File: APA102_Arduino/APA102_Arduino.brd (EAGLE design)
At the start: 39.4 x 32.8 mm, 16 parts, among them J1 POWER_JACKSMD, U1 V_REG_LD1117, U2 ATMEGA328P-PU

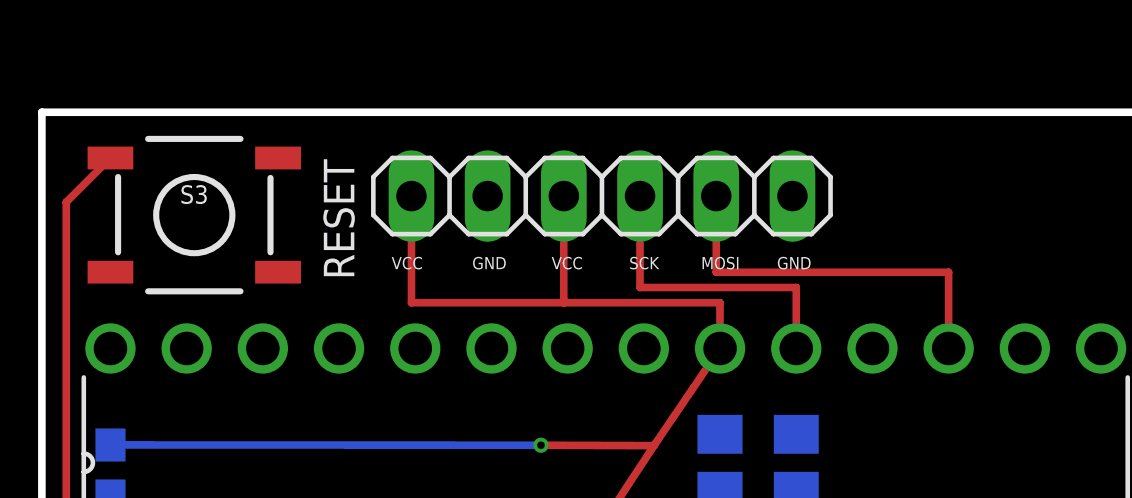
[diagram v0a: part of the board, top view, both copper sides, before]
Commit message: Updated design to use the 6-pin header autogenerated from Library.IO that includes a 3D package.
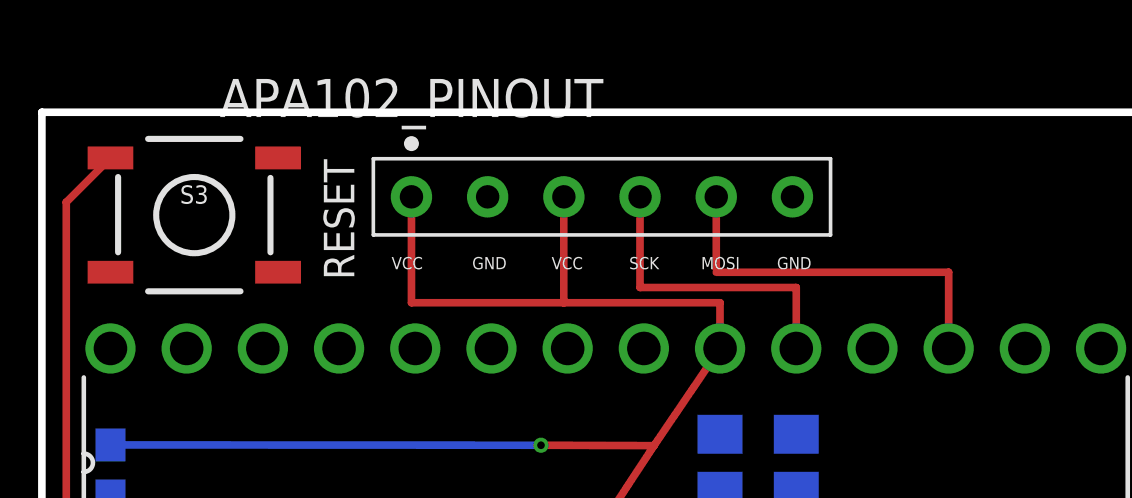
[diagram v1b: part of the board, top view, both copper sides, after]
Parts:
- APA102_PINOUT: value (none) -> 929974-01-06-RK9; device pinhead:1X06 -> SamacSys_Parts:929974-01-06-RK
- moved APA102_PINOUT 6.35 mm to (12.3, 29.9)

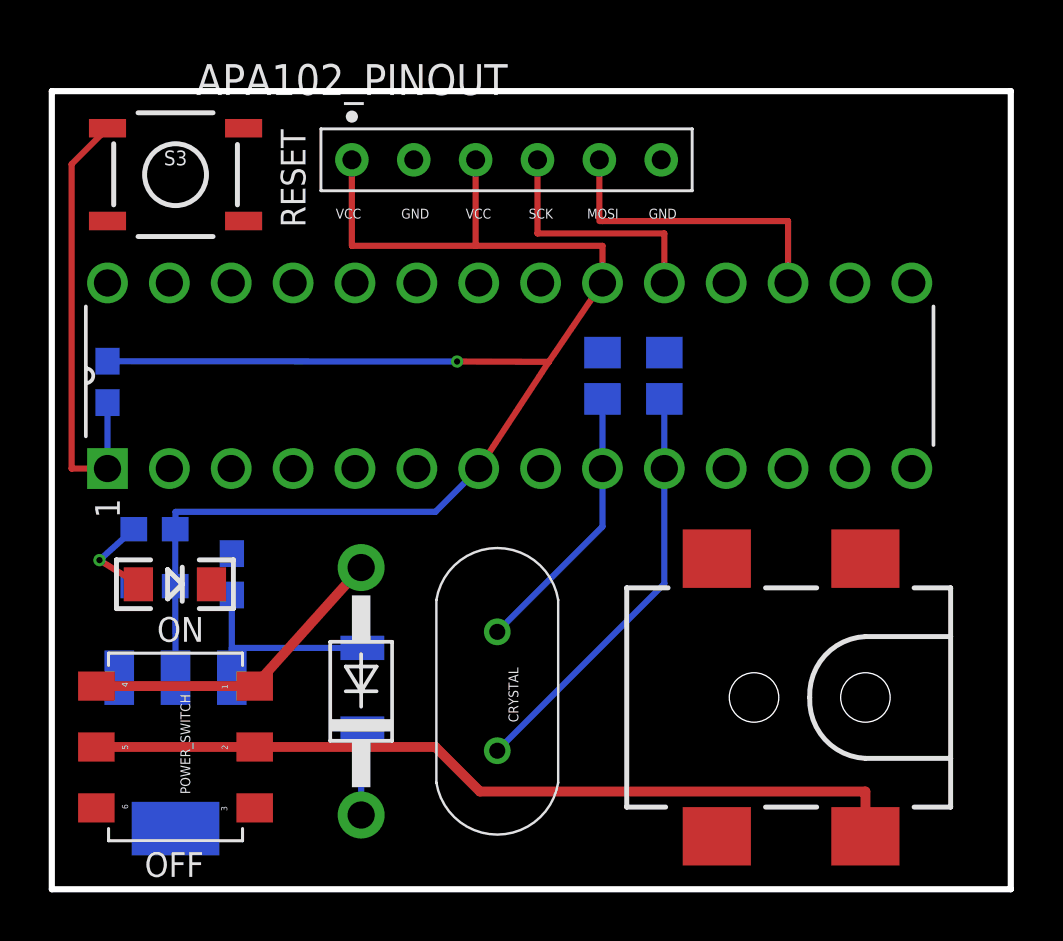
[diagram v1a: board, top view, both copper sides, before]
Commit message: Updated to include devices containing 3D Objects for crystal and power jack.
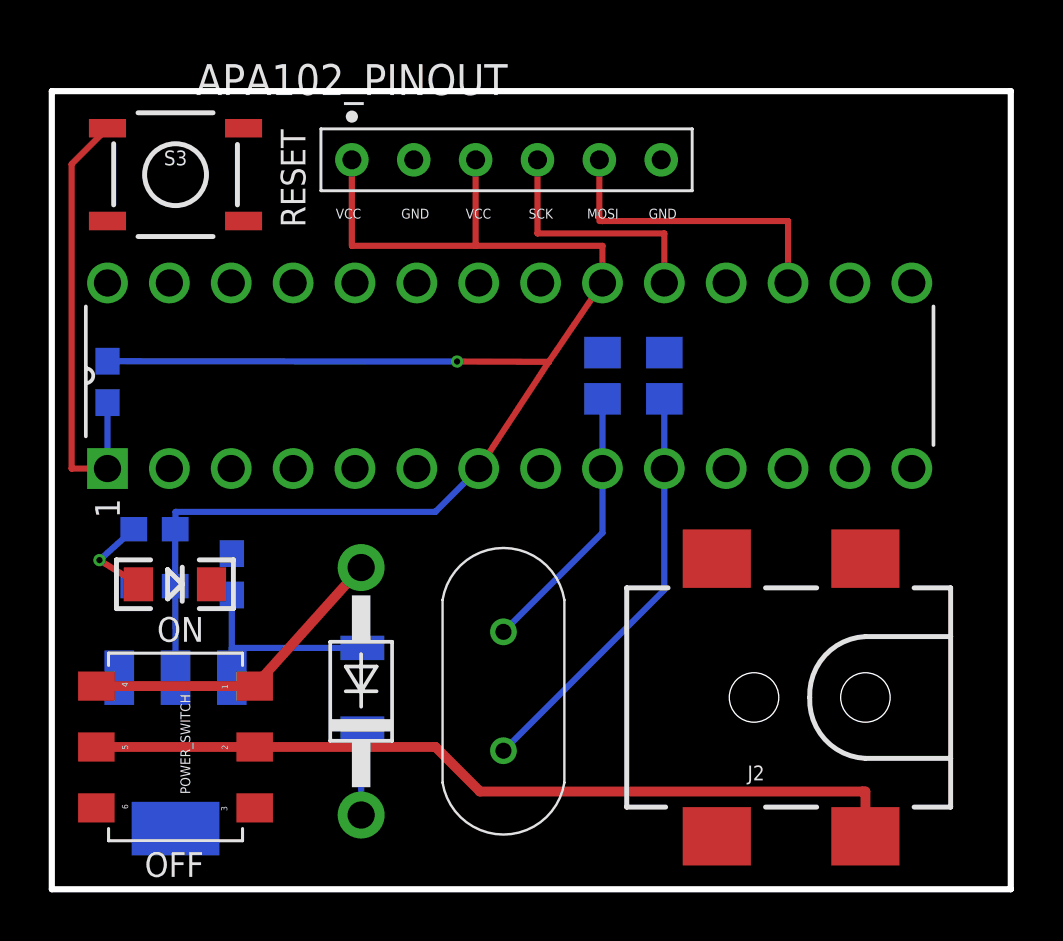
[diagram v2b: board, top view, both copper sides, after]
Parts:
- removed CRYSTAL: 16MHZ, SamacSys_Parts:HC/49US_(AT49)PTH
- removed J1: POWER_JACKSMD, SparkFun-Connectors:POWER_JACK_SMD
- added J2: POWER_JACKPOWER_JACK_SMD, Magister-Libraries:POWER_JACK_SMD
- added Y1: ABL-16.000MHZ-B4Y, Magister-Libraries:HC/49US_(AT49)PTH
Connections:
- net GND: now also J2.GND, J2.P$4; no longer J1.GND, J1.P$4
- net N$3: now also Y1.1; no longer CRYSTAL.2
- net N$6: now also Y1.2; no longer CRYSTAL.1
- net VIN: now also J2.VIN0; no longer J1.VIN0
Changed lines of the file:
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@@
 <drawing>
 <settings>
-<setting alwaysvectorfont="no"/>
+<setting alwaysvectorfont="yes"/>
 <setting keepoldvectorfont="yes"/>
 <setting verticaltext="up"/>
@@
 <layer number="59" name="tCarbon" color="7" fill="1" visible="no" active="no"/>
 <layer number="60" name="bCarbon" color="7" fill="1" visible="no" active="no"/>
+<layer number="88" name="SimResults" color="9" fill="1" visible="no" active="no"/>
+<layer number="89" name="SimProbes" color="9" fill="1" visible="no" active="no"/>
 <layer number="90" name="Modules" color="5" fill="1" visible="no" active="no"/>
 <layer number="91" name="Nets" color="2" fill="1" visible="no" active="no"/>
@@
 <layer number="112" name="tSilk" color="7" fill="1" visible="no" active="no"/>
 <layer number="113" name="IDFDebug" color="4" fill="1" visible="no" active="no"/>
+<layer number="114" name="Badge_Outline" color="7" fill="1" visible="no" active="no"/>
+<layer number="115" name="ReferenceISLANDS" color="7" fill="1" visible="no" active="no"/>
 <layer number="116" name="Patch_BOT" color="9" fill="4" visible="yes" active="yes"/>
+<layer number="117" name="PM_Ref" color="7" fill="1" visible="no" active="no"/>
 <layer number="118" name="Rect_Pads" color="7" fill="1" visible="no" active="no"/>
+<layer number="119" name="PF_Ref" color="7" fill="1" visible="no" active="no"/>
+<layer number="120" name="WFL_Ref" color="7" fill="1" visible="no" active="no"/>
 <layer number="121" name="_tsilk" color="7" fill="1" visible="yes" active="yes"/>
 <layer number="122" name="_bsilk" color="7" fill="1" visible="yes" active="yes"/>
@@
 <attribute name="VALUE" x="11.176" y="6.985" size="0.4064" layer="28" rot="MR90"/>
 </element>
-<element name="J1" library="SparkFun-Connectors" package="POWER_JACK_SMD" value="POWER_JACKSMD" x="33.401" y="7.874" smashed="yes" rot="R180">
-<attribute name="PROD_ID" value="CONN-08106" x="33.401" y="7.874" size="1.778" layer="27" rot="R180" display="off"/>
-</element>
 <element name="U2" library="ATMEGA328P-PU" package="DIP254P762X457-28" value="ATMEGA328P-PU" x="35.306" y="24.892" smashed="yes" rot="R90">
 <attribute name="AVAILABILITY" value="Unavailable" x="35.306" y="24.892" size="1.778" layer="27" rot="R90" display="off"/>
@@
 <attribute name="VALUE" x="27.5082" y="21.844" size="0.4064" layer="28" rot="MR270"/>
 </element>
-<element name="CRYSTAL" library="SamacSys_Parts" package="HC/49US_(AT49)PTH" value="16MHZ" x="18.288" y="8.128" smashed="yes" rot="R90">
-<attribute name="DESCRIPTION" value="Crystals 16.000MHZ, 18pF 30ppm -20C +70C" x="18.288" y="8.128" size="1.778" layer="27" rot="R90" display="off"/>
-<attribute name="HEIGHT" value="mm" x="18.288" y="8.128" size="1.778" layer="27" rot="R90" display="off"/>
-<attribute name="MANUFACTURER_NAME" value="ABRACON" x="18.288" y="8.128" size="1.778" layer="27" rot="R90" display="off"/>
-<attribute name="MANUFACTURER_PART_NUMBER" value="ABL-16.000MHz-B4Y" x="18.288" y="8.128" size="1.778" layer="27" rot="R90" display="off"/>
-<attribute name="MOUSER_PART_NUMBER" value="815-ABL-16-B4Y" x="18.288" y="8.128" size="1.778" layer="27" rot="R90" display="off"/>
-<attribute name="MOUSER_PRICE-STOCK" value="https://www.mouser.co.uk/ProductDetail/ABRACON/ABL-16000MHz-B4Y?qs=DZ%2FvJMgWWIsyUPmWNxNaQw%3D%3D" x="18.288" y="8.128" size="1.778" layer="27" rot="R90" display="off"/>
-<attribute name="NAME" x="18.9508" y="7.9822" size="0.4064" layer="25" rot="R270" align="center"/>
-<attribute name="RS_PART_NUMBER" value="" x="18.288" y="8.128" size="1.778" layer="27" rot="R90" display="off"/>
-<attribute name="RS_PRICE-STOCK" value="" x="18.288" y="8.128" size="1.778" layer="27" rot="R90" display="off"/>
-<attribute name="VALUE" x="18.3158" y="8.0584" size="0.4064" layer="27" rot="R270" align="center"/>
-</element>
 <element name="R5" library="SparkFun" package="0603-RES" value="10K" x="2.286" y="20.828" smashed="yes" rot="MR270">
 <attribute name="NAME" x="2.5146" y="22.4536" size="0.4064" layer="26" font="vector" rot="MR0"/>
@@
 <attribute name="VALUE" x="7.747" y="26.7716" size="1.27" layer="27" align="top-center"/>
 </element>
+<element name="Y1" library="Magister-Libraries" library_urn="urn:adsk.eagle:library:23190065" package="HC/49US_(AT49)PTH" package3d_urn="urn:adsk.eagle:package:23090764/3" value="ABL-16.000MHZ-B4Y" x="18.542" y="8.128" smashed="yes" rot="R270">
+<attribute name="DESCRIPTION" value="Crystals 16.000MHZ, 18pF 30ppm -20C +70C" x="18.542" y="8.128" size="1.778" layer="27" rot="R270" display="off"/>
+<attribute name="HEIGHT" value="mm" x="18.542" y="8.128" size="1.778" layer="27" rot="R270" display="off"/>
+<attribute name="MANUFACTURER_NAME" value="ABRACON" x="18.542" y="8.128" size="1.778" layer="27" rot="R270" display="off"/>
+<attribute name="MANUFACTURER_PART_NUMBER" value="ABL-16.000MHz-B4Y" x="18.542" y="8.128" size="1.778" layer="27" rot="R270" display="off"/>
+<attribute name="MOUSER_PART_NUMBER" value="815-ABL-16-B4Y" x="18.542" y="8.128" size="1.778" layer="27" rot="R270" display="off"/>
+<attribute name="MOUSER_PRICE-STOCK" value="https://www.mouser.co.uk/ProductDetail/ABRACON/ABL-16000MHz-B4Y?qs=DZ%2FvJMgWWIsyUPmWNxNaQw%3D%3D" x="18.542" y="8.128" size="1.778" layer="27" rot="R270" display="off"/>
+</element>
+<element name="J2" library="Magister-Libraries" library_urn="urn:adsk.eagle:library:23190065" package="POWER_JACK_SMD" package3d_urn="urn:adsk.eagle:package:23235900/2" value="POWER_JACKPOWER_JACK_SMD" x="33.401" y="7.874" smashed="yes" rot="R180">
+<attribute name="NAME" x="29.2608" y="5.08" size="0.6096" layer="25" font="vector" ratio="20" rot="R180"/>
+<attribute name="VALUE" x="29.591" y="11.176" size="0.6096" layer="27" font="vector" ratio="20" rot="R180"/>
+</element>
 </elements>
 <signals>
 <signal name="GND">
 <contactref element="LED2" pad="C"/>
-<contactref element="J1" pad="P$4"/>
-<contactref element="J1" pad="GND"/>
 <polygon width="0.254" layer="16" isolate="0.3048">
 <vertex x="0" y="32.766"/>
@@
 <contactref element="APA102_PINOUT" pad="2"/>
 <contactref element="APA102_PINOUT" pad="6"/>
+<contactref element="J2" pad="P$4"/>
+<contactref element="J2" pad="GND"/>
 </signal>
 <signal name="N$8">
@@
 </signal>
 <signal name="VIN">
-<contactref element="J1" pad="VIN0"/>
 <contactref element="POWER_SWITCH" pad="P2"/>
 <contactref element="POWER_SWITCH" pad="P5"/>
@@
 <wire x1="8.33" y1="5.842" x2="15.748" y2="5.842" width="0.4064" layer="1"/>
 <wire x1="15.748" y1="5.842" x2="17.5768" y2="4.0132" width="0.4064" layer="1"/>
-<wire x1="17.5768" y1="4.0132" x2="33.401" y2="4.0132" width="0.4064" layer="1"/>
+<wire x1="17.5768" y1="4.0132" x2="33.274" y2="4.0132" width="0.4064" layer="1"/>
+<contactref element="J2" pad="VIN0"/>
+<wire x1="33.274" y1="4.0132" x2="33.401" y2="4.0132" width="0.4064" layer="1"/>
 <wire x1="33.401" y1="4.0132" x2="33.401" y2="2.174" width="0.4064" layer="1"/>
 </signal>
 <signal name="N$3">
 <contactref element="U2" pad="9"/>
-<contactref element="CRYSTAL" pad="2"/>
 <contactref element="C4" pad="1"/>
-<wire x1="18.288" y1="10.568" x2="22.606" y2="14.886" width="0.254" layer="16"/>
-<wire x1="22.606" y1="14.886" x2="22.606" y2="17.272" width="0.254" layer="16"/>
 <wire x1="22.606" y1="17.272" x2="22.606" y2="20.132" width="0.254" layer="16"/>
+<contactref element="Y1" pad="1"/>
+<wire x1="22.606" y1="14.632" x2="18.542" y2="10.568" width="0.254" layer="16"/>
+<wire x1="22.606" y1="17.272" x2="22.606" y2="14.632" width="0.254" layer="16"/>
 </signal>
 <signal name="N$6">
 <contactref element="U2" pad="10"/>
-<contactref element="CRYSTAL" pad="1"/>
 <contactref element="C5" pad="1"/>
-<wire x1="18.288" y1="5.688" x2="25.146" y2="12.546" width="0.254" layer="16"/>
-<wire x1="25.146" y1="12.546" x2="25.146" y2="17.272" width="0.254" layer="16"/>
 <wire x1="25.146" y1="17.272" x2="25.146" y2="20.132" width="0.254" layer="16"/>
+<contactref element="Y1" pad="2"/>
+<wire x1="25.146" y1="12.292" x2="18.542" y2="5.688" width="0.254" layer="16"/>
+<wire x1="25.146" y1="17.272" x2="25.146" y2="12.292" width="0.254" layer="16"/>
 </signal>
 <signal name="N$7">
@@
 </signals>
 <mfgpreviewcolors>
-<mfgpreviewcolor name="soldermaskcolor" color="0xC8008000"/>
+<mfgpreviewcolor name="soldermaskcolor" color="0xC834009C"/>
 <mfgpreviewcolor name="silkscreencolor" color="0xFFFEFEFE"/>
 <mfgpreviewcolor name="backgroundcolor" color="0xFF282828"/>
@@
 which will not be processed correctly with this version.
 </note>
+<note version="8.2" severity="warning">
+Since Version 8.2, EAGLE supports online libraries. The ids
+of those online libraries will not be understood (or retained)
+with this version.
+</note>
 <note version="8.3" severity="warning">
